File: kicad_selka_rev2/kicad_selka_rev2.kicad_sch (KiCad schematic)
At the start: 104 parts, among them J1 Conn_01x02_Pin, J10 Conn_01x01_Pin, J11 Conn_01x01_Pin, J12 Conn_01x01_Pin, J13 Conn_01x01_Pin, J14 Conn_01x01_Pin, J15 Conn_01x01_Pin, J16 Conn_01x01_Pin, J17 Conn_01x01_Pin, J18 Conn_01x01_Pin, J19 Conn_01x01_Pin, J2 Conn_01x01_Pin, J20 Conn_01x01_Pin, J3 Conn_01x01_Pin, J4 Conn_01x06_Pin, J5 Conn_01x01_Pin, J6 Conn_01x01_Pin, J7 Conn_01x01_Pin, J8 Conn_01x01_Pin, J9 Conn_01x01_Pin, Q1 NPN, U1 ATtiny861A-S

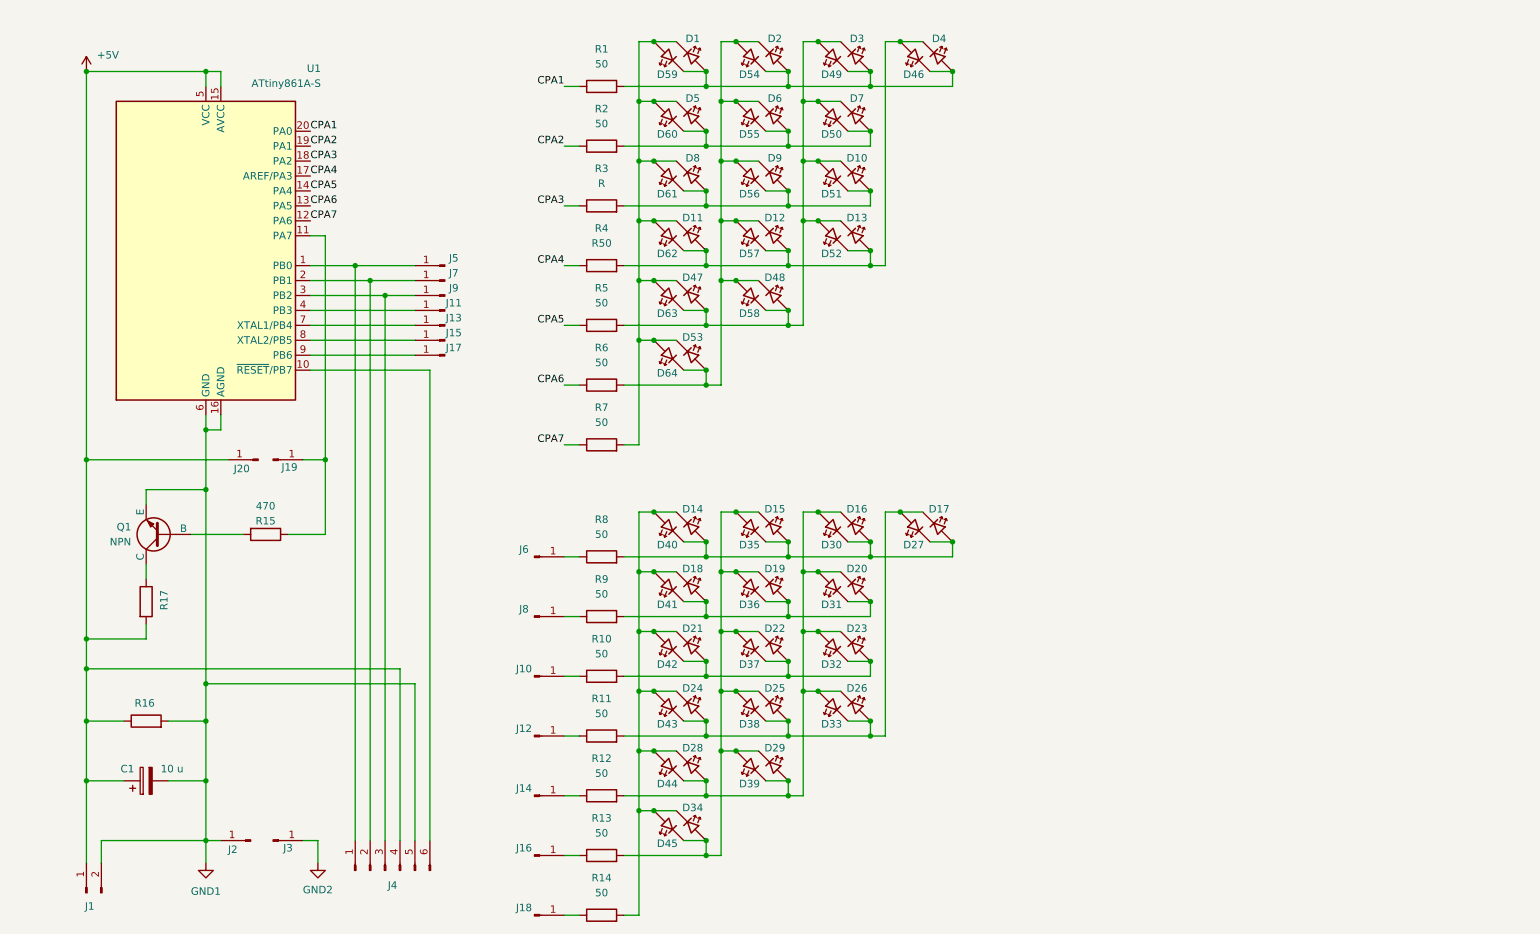
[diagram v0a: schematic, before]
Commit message: Lisää putsausta ja selkäsalaman muutosta
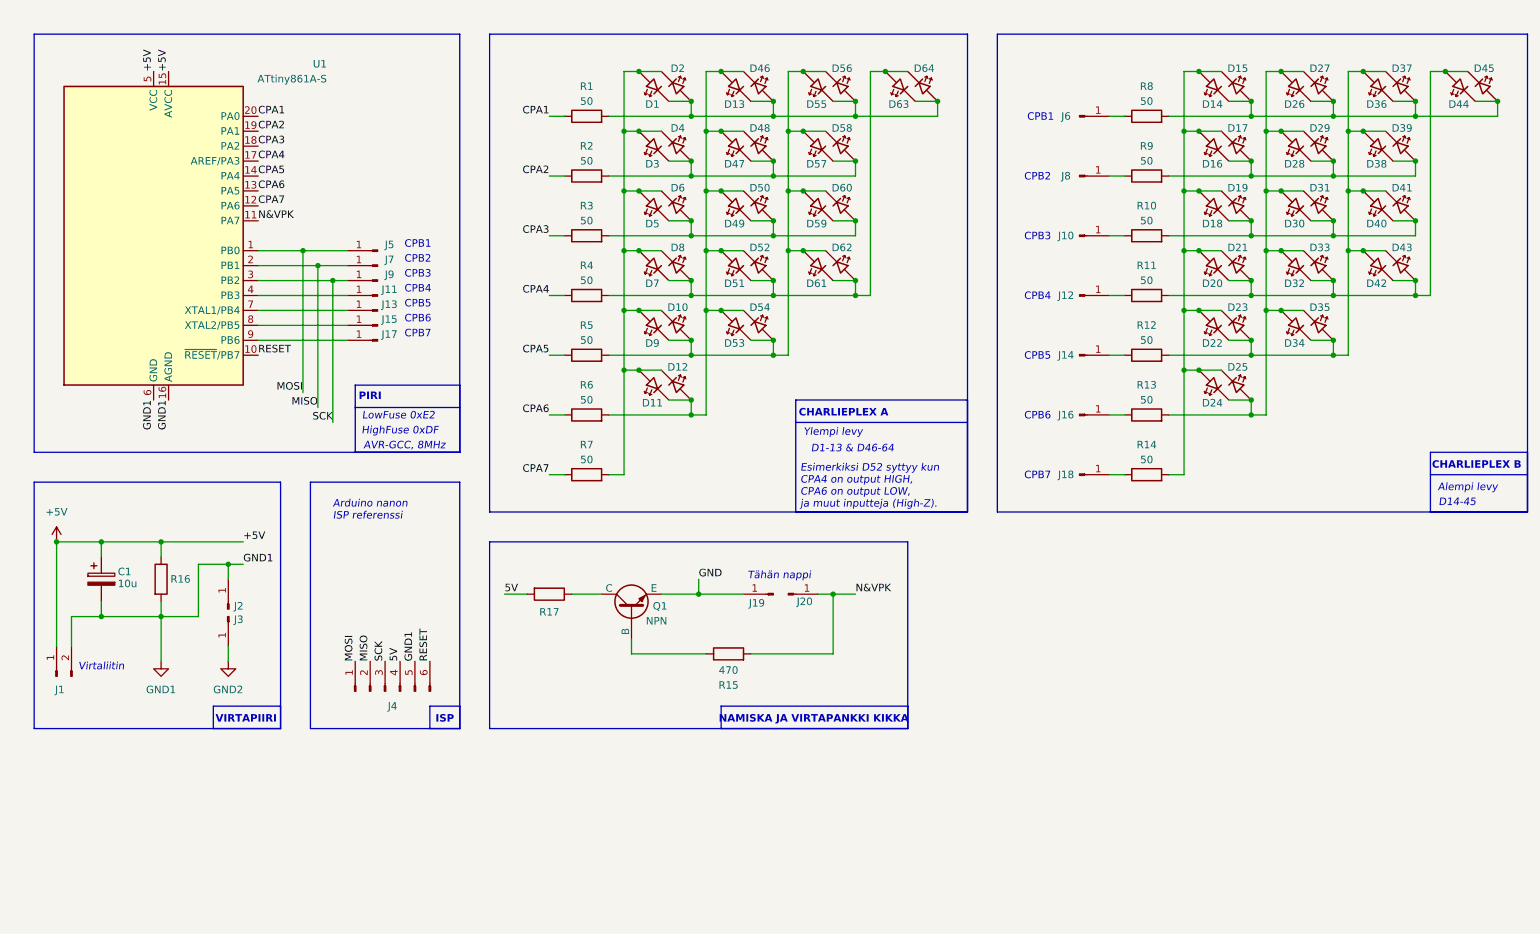
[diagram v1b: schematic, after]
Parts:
- C1: value 10 u -> 10u
- J4: footprint Connector_PinHeader_2.00mm:PinHeader_1x06_P2.00mm_Horizontal -> Library_zani:PinHeader_1x06_P2.00mm_Horizontal_with_SMD
- R1, R10, R11, R12, R13, R14, R2, R5, R6, R7, R8, R9: footprint Resistor_SMD:R_1206_3216Metric_Pad1.30x1.75mm_HandSolder -> Resistor_SMD:R_1210_3225Metric_Pad1.30x2.65mm_HandSolder
- R3: value R -> 50; footprint Resistor_SMD:R_1206_3216Metric_Pad1.30x1.75mm_HandSolder -> Resistor_SMD:R_1210_3225Metric_Pad1.30x2.65mm_HandSolder
- R4: value R50 -> 50; footprint Resistor_SMD:R_1206_3216Metric_Pad1.30x1.75mm_HandSolder -> Resistor_SMD:R_1210_3225Metric_Pad1.30x2.65mm_HandSolder
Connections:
- net +5V: no longer J20.1 (Pin_1), J4.4 (Pin_4), R17.2
- net GND1: no longer Q1.3 (E)
- net at Q1.2 (B): now also R15.1; no longer R15.2
- net MOSI: now reaches J4.1 (Pin_1), J5.1 (Pin_1), U1.1 (PB0)
- net RESET: now reaches J4.6 (Pin_6), U1.10 (~{RESET}/PB7)
- net MISO: now reaches J4.2 (Pin_2), J7.1 (Pin_1), U1.2 (PB1)
- net SCK: now reaches J4.3 (Pin_3), J9.1 (Pin_1), U1.3 (PB2)
- new net: D16.1 (K), D17.2 (A), D28.1 (K), D29.2 (A), D38.1 (K), D39.2 (A), R9.2
- new net: D22.1 (K), D23.2 (A), D34.1 (K), D35.2 (A), D36.2 (A), D37.1 (K), D38.2 (A), D39.1 (K), D40.2 (A), D41.1 (K), D42.2 (A), D43.1 (K), R12.2
- new net: D10.2 (A), D53.1 (K), D54.2 (A), D55.2 (A), D56.1 (K), D57.2 (A), D58.1 (K), D59.2 (A), D60.1 (K), D61.2 (A), D62.1 (K), D9.1 (K), R5.2
- new net: D11.1 (K), D12.2 (A), D13.2 (A), D46.1 (K), D47.2 (A), D48.1 (K), D49.2 (A), D50.1 (K), D51.2 (A), D52.1 (K), D53.2 (A), D54.1 (K), R6.2
- new net: D1.1 (K), D13.1 (K), D2.2 (A), D46.2 (A), D55.1 (K), D56.2 (A), D63.1 (K), D64.2 (A), R1.2
- new net: D49.1 (K), D5.1 (K), D50.2 (A), D59.1 (K), D6.2 (A), D60.2 (A), R3.2
- new net: D1.2 (A), D10.1 (K), D11.2 (A), D12.1 (K), D2.1 (K), D3.2 (A), D4.1 (K), D5.2 (A), D6.1 (K), D7.2 (A), D8.1 (K), D9.2 (A), R7.2
- new net: D14.2 (A), D15.1 (K), D16.2 (A), D17.1 (K), D18.2 (A), D19.1 (K), D20.2 (A), D21.1 (K), D22.2 (A), D23.1 (K), D24.2 (A), D25.1 (K), R14.2
- new net: D3.1 (K), D4.2 (A), D47.1 (K), D48.2 (A), D57.1 (K), D58.2 (A), R2.2
- new net: D18.1 (K), D19.2 (A), D30.1 (K), D31.2 (A), D40.1 (K), D41.2 (A), R10.2
- new net: D51.1 (K), D52.2 (A), D61.1 (K), D62.2 (A), D63.2 (A), D64.1 (K), D7.1 (K), D8.2 (A), R4.2
- new net: D14.1 (K), D15.2 (A), D26.1 (K), D27.2 (A), D36.1 (K), D37.2 (A), D44.1 (K), D45.2 (A), R8.2
- new net: D20.1 (K), D21.2 (A), D32.1 (K), D33.2 (A), D42.1 (K), D43.2 (A), D44.2 (A), D45.1 (K), R11.2
- new net: D24.1 (K), D25.2 (A), D26.2 (A), D27.1 (K), D28.2 (A), D29.1 (K), D30.2 (A), D31.1 (K), D32.2 (A), D33.1 (K), D34.2 (A), D35.1 (K), R13.2
- new net 5V: J4.4 (Pin_4), R17.2
- new net GND: J19.1 (Pin_1), Q1.3 (E)
- new net N&VPK: J20.1 (Pin_1), R15.2, U1.11 (PA7)
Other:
- note added: "AVR-GCC, 8MHz"
- note added: "Alempi levy"
- note added: "Arduino nanon ISP referenssi"
- note added: "CHARLIEPLEX A"
- note added: "CHARLIEPLEX B"
- note added: "CPB1"
- note added: "CPB2"
- note added: "CPB3"
- note added: "CPB4"
- note added: "CPB5"
- note added: "CPB6"
- note added: "CPB7"
- note added: "D1-13 & D46-64"
- note added: "D14-45"
- note added: "Esimerkiksi D52 syttyy kun CPA4 on output HIGH, CPA6 on output LOW, ja muut inputteja (High-Z)."
- note added: "HighFuse 0xDF"
- note added: "ISP"
- note added: "LowFuse 0xE2"
- note added: "NAMISKA JA VIRTAPANKKI KIKKA"
- note added: "PIRI"
- note added: "Tähän nappi"
- note added: "VIRTAPIIRI"
- note added: "Virtaliitin"
- note added: "Ylempi levy"
- moved on the sheet: C1, J1, J10, J11, J12, J13, J14, J15, J16, J17, J18, J19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

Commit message: hiomista vaille rev
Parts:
- removed J1: Conn_01x02_Pin, Connector_PinHeader_2.00mm:PinHeader_1x02_P2.00mm_Vertical, symbol Connector:Conn_01x02_Pin
- removed J10, J11, J12, J13, J14, J15, J16, J17, J18, J19, J2, J20, J3, J5, J6, J7, J8, J9: Conn_01x01_Pin, Connector_PinHeader_2.00mm:PinHeader_1x01_P2.00mm_Vertical, symbol Connector:Conn_01x01_Pin
- removed J4: Conn_01x06_Pin, Library_zani:PinHeader_1x06_P2.00mm_Horizontal_with_SMD, symbol Connector:Conn_01x06_Pin
- removed Q1: NPN, Package_TO_SOT_SMD:SOT-23_Handsoldering, symbol Simulation_SPICE:NPN
- removed R15: 470, Resistor_SMD:R_1206_3216Metric_Pad1.30x1.75mm_HandSolder, symbol Device:R
- removed R17: X, Resistor_SMD:R_1206_3216Metric_Pad1.30x1.75mm_HandSolder, symbol Device:R
- removed U1: ATtiny861A-S, Package_SO:SOIC-20W_7.5x12.8mm_P1.27mm, symbol MCU_Microchip_ATtiny:ATtiny861A-S
- added C2, C3: 100n, Capacitor_SMD:C_0805_2012Metric_Pad1.18x1.45mm_HandSolder, symbol Device:C_Small
- added J1: Conn_01x02, Connector_PinHeader_2.54mm:PinHeader_1x02_P2.54mm_Vertical, symbol Connector_Generic:Conn_01x02
- added J2: Conn_01x06, footprintteja:PinHeader_1x06_P2.00mm_Horizontal_smd_tht, symbol Connector_Generic:Conn_01x06
- added J3, J4: Conn_01x08, footprintteja:PinHeader_1x08_P2.00mm_Vertical_levee, symbol Connector_Generic:Conn_01x08
- added SW1: PUSH, Connector_PinHeader_2.00mm:PinHeader_1x02_P2.00mm_Vertical, symbol Switch:SW_Push
- added U1: ATtiny861A SOIC20, Package_SO:SOIC-20W_7.5x12.8mm_P1.27mm, symbol ATtiny_861A:ATtiny861A-S
- R15: renamed from R16; footprint Resistor_SMD:R_1206_3216Metric_Pad1.30x1.75mm_HandSolder -> Resistor_SMD:R_1210_3225Metric_Pad1.30x2.65mm_HandSolder
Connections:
- net +5V: now also C2.1, C3.1, J1.1 (Pin_1), J2.4 (Pin_4), U1.15 (AVCC), U1.5 (VCC)
- net GND1: now also C2.2, C3.2, J1.2 (Pin_2), J2.5 (Pin_5), J3.8 (Pin_8), SW1.1, U1.16 (AGND), U1.6 (GND)
- net GND2: now also J4.8 (Pin_8)
- net CB6: now reaches R14.1
- net CB6: now also J4.7 (Pin_7)
- net at D1.1 (K), D13.1 (K), D2.2 (A)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: now also D63.2 (A), D64.1 (K); no longer D63.1 (K), D64.2 (A)
- net CB2: now reaches R10.1
- net CB2: now also J4.3 (Pin_3)
- net at D51.1 (K), D52.2 (A), D61.1 (K)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: now also D63.1 (K), D64.2 (A); no longer D63.2 (A), D64.1 (K)
- net CB3: now reaches R11.1
- net CB3: now also J4.4 (Pin_4)
- net CB1: now reaches R9.1
- net CB1: now also J4.2 (Pin_2)
- net CB0: now reaches R8.1
- net CB0: now also J4.1 (Pin_1)
- net CB4: now reaches R12.1
- net CB4: now also J4.5 (Pin_5)
- net CB5: now reaches R13.1
- net CB5: now also J4.6 (Pin_6)
- net CPA1 renamed CA0
- net CA0: now also U1.20 (PA0)
- net CPA2 renamed CA1
- net CA1: now also U1.19 (PA1)
- net CPA3 renamed CA2
- net CA2: now also U1.18 (PA2)
- net CPA4 renamed CA3
- net CA3: now also U1.17 (AREF/PA3)
- net CPA5 renamed CA4
- net CA4: now also U1.14 (PA4)
- net CPA6 renamed CA5
- net CA5: now also U1.13 (PA5)
- net CPA7 renamed CA6
- net CA6: now also U1.12 (PA6)
- new net: SW1.2, U1.11 (PA7)
- new net PB0: J2.1 (Pin_1), J3.1 (Pin_1), U1.1 (PB0)
- new net PB1: J2.2 (Pin_2), J3.2 (Pin_2), U1.2 (PB1)
- new net PB2: J2.3 (Pin_3), J3.3 (Pin_3), U1.3 (PB2)
- new net PB3: J3.4 (Pin_4), U1.4 (PB3)
- new net PB4: J3.5 (Pin_5), U1.7 (XTAL1/PB4)
- new net PB5: J3.6 (Pin_6), U1.8 (XTAL2/PB5)
- new net PB6: J3.7 (Pin_7), U1.9 (PB6)
- new net PB7: J2.6 (Pin_6), U1.10 (~{RESET}/PB7)
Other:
- note added: "1 -> 1 2 -> 2 3 -> 3 jne."
- note added: "AVR ISP"
- note added: "Esimerkiksi D52 syttyy kun PA3 (CA3) on output HIGH, PA5 (CA5) on output LOW, ja muut inputteja (High-Z)."
- note added: "HYPPYJOHDOT"
- note added: "LowFuse 0xE2 HighFuse 0xDF @8MHz"
- note removed: "AVR-GCC, 8MHz"
- note removed: "Arduino nanon ISP referenssi"
- note removed: "CPB1"
- note removed: "CPB2"
- note removed: "CPB3"
- note removed: "CPB4"
- note removed: "CPB5"
- note removed: "CPB6"
- note removed: "CPB7"
- note removed: "Esimerkiksi D52 syttyy kun CPA4 on output HIGH, CPA6 on output LOW, ja muut inputteja (High-Z)."
- note removed: "HighFuse 0xDF"
- note removed: "ISP"
- note removed: "LowFuse 0xE2"
- note removed: "NAMISKA JA VIRTAPANKKI KIKKA"
- note removed: "Tähän nappi"
- note removed: "Virtaliitin"
- moved on the sheet: C1, D1, D10, D11, D12, D13, D14, D15, D16, D17, D18, D19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
